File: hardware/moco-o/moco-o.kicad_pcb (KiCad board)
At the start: 4 copper layers, 58 x 52.5 mm, 203 parts, among them J1 USB_C_Receptacle_USB2.0, J10 Conn_01x03, J11 Conn_02x02_Top_Bottom, J12 Conn_02x02_Top_Bottom, J13 Conn_01x02, J2 Conn_02x10_Odd_Even, J3 Conn_01x02, J4 Conn_01x05, J5 SWD 10-Pin, J6 ST-LINK, J8 Conn_01x06, J9 Conn_01x06, Q1 AO3413, Q10 CSD18540Q5B, Q2 AO3413, Q3 CSD18540Q5B, Q4 CSD18540Q5B, Q5 CSD18540Q5B, Q6 CSD18540Q5B, Q7 CSD18540Q5B, Q8 CSD18540Q5B, Q9 CSD18540Q5B, SW1 SW_Push, SW2 SW_Push, SW3 SW_Push, SW4 SW_Push, U1 AMS1117-3.3, U2 DRV8301, U3 8MHz, U4 STM32F405RGTx, U5 TJA1051T-3, U6 LM5109A, U7 AS5047x

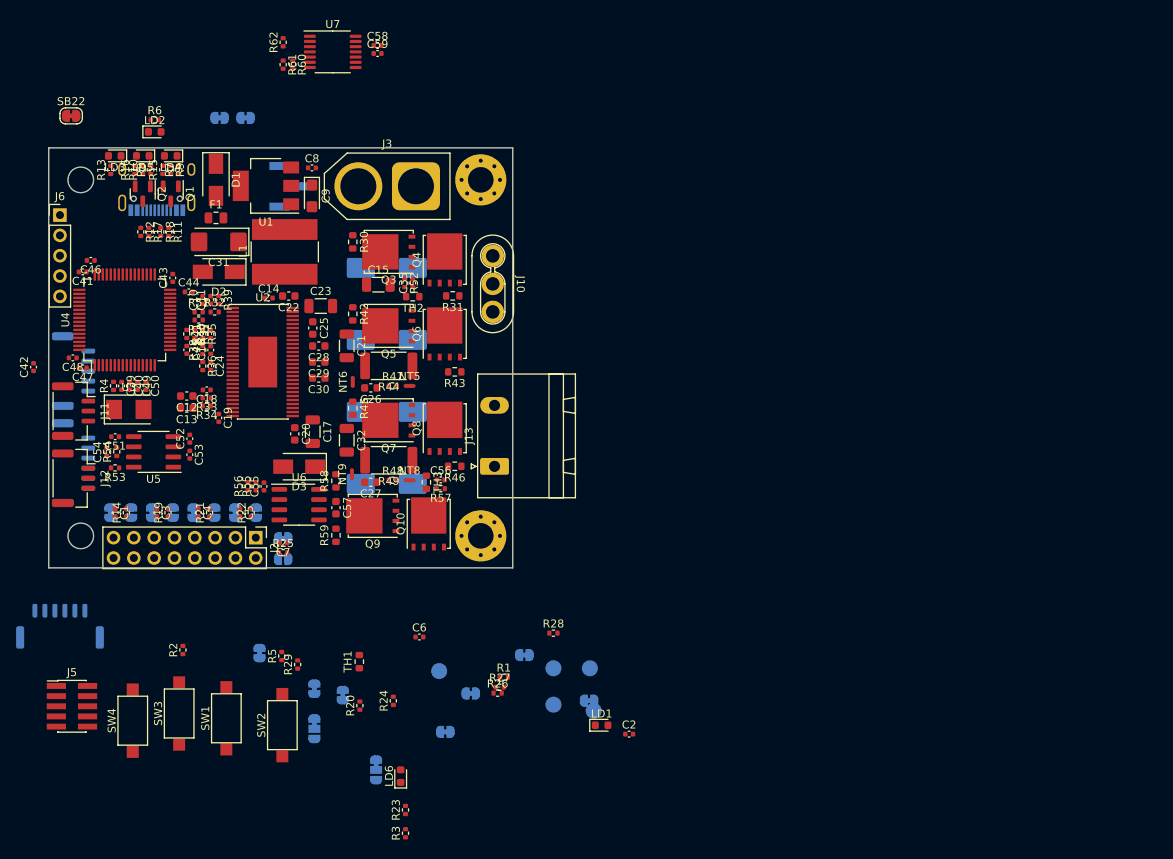
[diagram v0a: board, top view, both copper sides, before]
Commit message: Change to DRV8323H
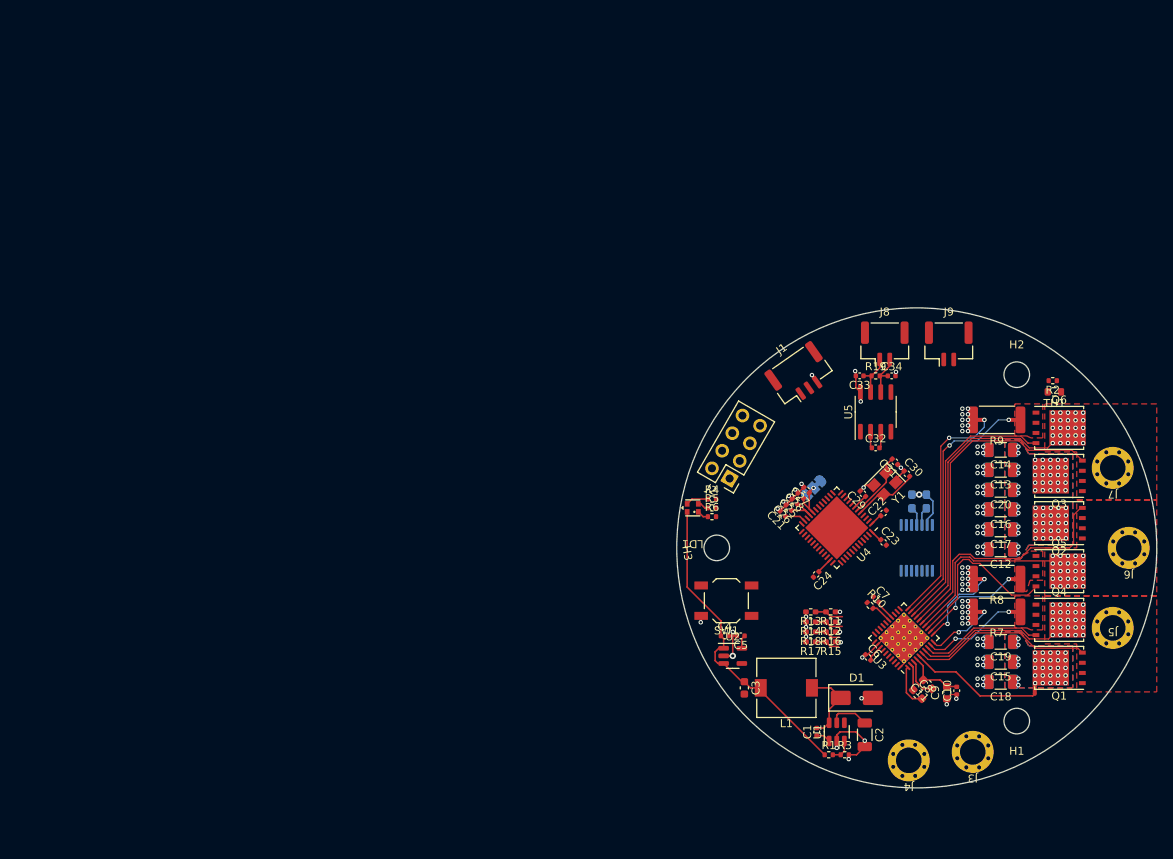
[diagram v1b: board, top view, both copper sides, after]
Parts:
- removed C46: 2.2uF/25V, Capacitor_SMD:C_0402_1005Metric
- removed C47, C48, C49, C51, C53, C59: 100nF, Capacitor_SMD:C_0402_1005Metric
- removed C50: 1uF/25V, Capacitor_SMD:C_0402_1005Metric
- removed C52: 47uF, Capacitor_SMD:C_0402_1005Metric
- removed C54: 100pF, Capacitor_SMD:C_0402_1005Metric
- removed C55, C56: 2.2uF, Capacitor_SMD:C_0402_1005Metric
- removed C57: 100nF/50V, Capacitor_SMD:C_0603_1608Metric
- removed C58: 1uF, Capacitor_SMD:C_0402_1005Metric
- removed D2, D3: SS34, Diode_SMD:D_SMA
- removed F1: 500mA/6V, Fuse:Fuse_0805_2012Metric
- removed H4: MountingHole, MountingHole:MountingHole_3.2mm_M3_ISO14580
- removed J10: Conn_01x03, moco:AMASS MR30PB-F
- removed J11, J12: Conn_02x02_Top_Bottom, Connector_JST:JST_GH_SM03B-GHS-TB_1x03-1MP_P1.25mm_Horizontal
- removed J13: Conn_01x02, Connector_Phoenix_GMSTB:PhoenixContact_GMSTBA_2,5_2-G-7,62_1x02_P7.62mm_Horizontal
- removed JP1: Jumper_3_Open, Connector_PinHeader_2.54mm:PinHeader_1x03_P2.54mm_Vertical_SMD_Pin1Left
- removed LD2, LD3, LD4, LD5, LD6: LED, LED_SMD:LED_0603_1608Metric
- removed NT8, NT9: NetTie_2, NetTie:NetTie-2_SMD_Pad0.5mm
- removed Q10, Q7, Q8, Q9: CSD18540Q5B, Package_TO_SOT_SMD:TDSON-8-1
- removed R20, R23, R35, R37, R41, R52, R53, R57, R60, R61, R62: 10k, Resistor_SMD:R_0402_1005Metric
- removed R21, R22, R25, R26, R27, R28, R38, R51, R55, R56: 3.3k, Resistor_SMD:R_0402_1005Metric
- removed R24, R29, R36: 1k, Resistor_SMD:R_0402_1005Metric
- removed R30, R31, R42, R43, R45, R46, R58, R59: 2.2R, Resistor_SMD:R_0603_1608Metric
- removed R32: 47k, Resistor_SMD:R_0402_1005Metric
- removed R33, R34: 22R, Resistor_SMD:R_0402_1005Metric
- removed R39: 220k 1%, Resistor_SMD:R_0402_1005Metric
- removed R40, R50: 18k, Resistor_SMD:R_0402_1005Metric
- removed R44, R49: 0.5mΩ, Resistor_SMD:R_2512_6332Metric
- removed R47, R48, R54: 120R, Resistor_SMD:R_0402_1005Metric
- removed SB10, SB12, SB14, SB16, SB8: SolderJumper_2_Open, Jumper:SolderJumper-2_P1.3mm_Open_RoundedPad1.0x1.5mm
- removed SB11, SB13, SB15, SB17, SB19, SB2, SB20, SB22, SB3, SB4, SB5, SB6, SB7, SB9: SolderJumper_2_Bridged, Jumper:SolderJumper-2_P1.3mm_Bridged_RoundedPad1.0x1.5mm
- removed SB18, SB21: SolderJumper_3_Bridged12, Jumper:SolderJumper-3_P1.3mm_Bridged12_RoundedPad1.0x1.5mm_NumberLabels
- removed SW2, SW3, SW4: SW_Push, Button_Switch_SMD:SW_SPST_CK_RS282G05A3
- removed TH2, TH3: NCP18XH103F03RB, Resistor_SMD:R_0603_1608Metric
- removed TP1, TP2: TestPoint_Small, TestPoint:TestPoint_Pad_D2.0mm
- removed TP3, TP4, TP5: TestPoint, TestPoint:TestPoint_Pad_D2.0mm
- removed U7: AS5047x, Package_SO:TSSOP-14_4.4x5mm_P0.65mm
- added C38: 10uF/50V, Capacitor_SMD:C_1206_3216Metric_Pad1.33x1.80mm_HandSolder, B.Cu at (160.5, 90.2)
- added J7: C, moco:wire_3.2mm, F.Cu at (174.5, 90.0)
- added NT1: NetTie_2, NetTie:NetTie-2_SMD_Pad0.5mm, F.Cu at (162.0, 108.0)
- added NT2: NetTie_2, NetTie:NetTie-2_SMD_Pad0.5mm, F.Cu at (162.0, 103.9)
- added NT3: NetTie_2, NetTie:NetTie-2_SMD_Pad0.5mm, F.Cu at (162.0, 84.0)
- added NT4: NetTie_2, NetTie:NetTie-2_SMD_Pad0.5mm, F.Cu at (158.0, 108.0)
- added NT7: NetTie_2, NetTie:NetTie-2_SMD_Pad0.5mm, F.Cu at (164.8, 117.8)
- added Y1: 8MHz, Crystal:Crystal_SMD_3225-4Pin_3.2x2.5mm, F.Cu at (146.0, 92.0)
- C1: value 82pF -> 100nF
- C10: value 270pF -> 100nF
- C11: value 82pF -> 1uF/16V; footprint Capacitor_SMD:C_0402_1005Metric -> Capacitor_SMD:C_0603_1608Metric
- C12, C13: value 2.2nF -> 10uF/50V; footprint Capacitor_SMD:C_0603_1608Metric -> Capacitor_SMD:C_1206_3216Metric
- C14: value 15nF -> 10uF/50V; footprint Capacitor_SMD:C_0402_1005Metric -> Capacitor_SMD:C_1206_3216Metric
- C15: value 2.2uF/100V -> 10uF/50V
- C16: value 2.2uF -> 10uF/50V; footprint Capacitor_SMD:C_0402_1005Metric -> Capacitor_SMD:C_1206_3216Metric
- C17: value 4.7uF/50V -> 10uF/50V
- C18, C19: value 1uF -> 10uF/50V; footprint Capacitor_SMD:C_0402_1005Metric -> Capacitor_SMD:C_1206_3216Metric
- C2: value 2.2uF -> 1uF/50V; footprint Capacitor_SMD:C_0402_1005Metric -> Capacitor_SMD:C_1206_3216Metric
- C20: value 100nF/50V -> 10uF/50V; footprint Capacitor_SMD:C_0603_1608Metric -> Capacitor_SMD:C_1206_3216Metric
- C21, C32: value 2.2uF/100V -> 100nF; footprint Capacitor_SMD:C_1206_3216Metric -> Capacitor_SMD:C_0402_1005Metric
- C22, C28, C29: value 100nF/50V -> 100nF; footprint Capacitor_SMD:C_0603_1608Metric -> Capacitor_SMD:C_0402_1005Metric
- C23: value 4.7uF/50V -> 100nF; footprint Capacitor_SMD:C_1206_3216Metric -> Capacitor_SMD:C_0402_1005Metric
- C24: value 22nF -> 100nF
- C25: value 100nF/50V -> 10nF; footprint Capacitor_SMD:C_0603_1608Metric -> Capacitor_SMD:C_0402_1005Metric
- C26, C27: value 2.2nF -> 1uF; footprint Capacitor_SMD:C_0603_1608Metric -> Capacitor_SMD:C_0402_1005Metric
- C3: value 82pF -> 10uF; footprint Capacitor_SMD:C_0402_1005Metric -> Capacitor_SMD:C_0603_1608Metric
- C30: value 100nF/50V -> 12pF; footprint Capacitor_SMD:C_0603_1608Metric -> Capacitor_SMD:C_0402_1005Metric
- C31: value 68uF -> 12pF; footprint Capacitor_Tantalum_SMD:CP_EIA-6032-28_Kemet-C -> Capacitor_SMD:C_0402_1005Metric
- C33, C34: value 47uF/63V -> 30pF; footprint Capacitor_SMD:CP_Elec_8x10 -> Capacitor_SMD:C_0402_1005Metric; moved to F.Cu
- C35: value 2.2uF -> 100nF; footprint Capacitor_SMD:C_0402_1005Metric -> Capacitor_SMD:C_0603_1608Metric_Pad1.08x0.95mm_HandSolder; moved to B.Cu
- C36: value 47uF/63V -> 1uF; footprint Capacitor_SMD:CP_Elec_8x10 -> Capacitor_SMD:C_0603_1608Metric_Pad1.08x0.95mm_HandSolder
- C37: value 47uF/63V -> 10uF/50V; footprint Capacitor_SMD:CP_Elec_8x10 -> Capacitor_SMD:C_1206_3216Metric_Pad1.33x1.80mm_HandSolder
- C39, C40: value 20pF -> 10uF/50V; footprint Capacitor_SMD:C_0402_1005Metric -> Capacitor_SMD:C_1206_3216Metric_Pad1.33x1.80mm_HandSolder; moved to B.Cu
- C4, C5: value 82pF -> 1uF
- C41, C42, C43, C45: value 100nF -> 10uF/50V; footprint Capacitor_SMD:C_0402_1005Metric -> Capacitor_SMD:C_1206_3216Metric_Pad1.33x1.80mm_HandSolder; moved to B.Cu
- C44: value 2.2uF/25V -> 10uF/50V; footprint Capacitor_SMD:C_0402_1005Metric -> Capacitor_SMD:C_1206_3216Metric_Pad1.33x1.80mm_HandSolder; moved to B.Cu
- C6: value 270pF -> 1uF/6.3V
- C7: value 82pF -> 100nF/6.3V
- C8: value 10uF -> 47nF; footprint Capacitor_SMD:C_0402_1005Metric -> Capacitor_SMD:C_0603_1608Metric
- C9: footprint Capacitor_Tantalum_SMD:CP_EIA-3216-18_Kemet-A -> Capacitor_SMD:C_0603_1608Metric
- H1, H2: value MountingHole_Pad -> MountingHole; footprint MountingHole:MountingHole_3.2mm_M3_Pad_Via -> MountingHole:MountingHole_3.2mm_M3_ISO14580
- J1: value USB_C_Receptacle_USB2.0 -> Serial; footprint Connector_USB:USB_C_Receptacle_HRO_TYPE-C-31-M-12 -> Connector_JST:JST_GH_BM03B-GHS-TBT_1x03-1MP_P1.25mm_Vertical; moved to F.Cu
- J2: value Conn_02x10_Odd_Even -> Debug; footprint Connector_PinHeader_2.54mm:PinHeader_2x08_P2.54mm_Vertical -> Connector_PinHeader_2.54mm:PinHeader_2x04_P2.54mm_Vertical
- J3: value Conn_01x02 -> A; footprint Connector_AMASS:AMASS_XT60-M_1x02_P7.20mm_Vertical -> moco:wire_3.2mm
- J4: value Conn_01x05 -> A; footprint Connector_JST:JST_GH_SM05B-GHS-TB_1x05-1MP_P1.25mm_Horizontal -> moco:wire_3.2mm; moved to F.Cu
- J5: value SWD 10-Pin -> A; footprint Connector_PinHeader_1.27mm:PinHeader_2x05_P1.27mm_Vertical_SMD -> moco:wire_3.2mm
- J6: value ST-LINK -> B; footprint Connector_PinHeader_2.54mm:PinHeader_1x05_P2.54mm_Vertical -> moco:wire_3.2mm
- J8: value Conn_01x06 -> CAN1; footprint Connector_JST:JST_GH_SM06B-GHS-TB_1x06-1MP_P1.25mm_Horizontal -> Connector_JST:JST_GH_BM02B-GHS-TBT_1x02-1MP_P1.25mm_Vertical; moved to F.Cu
- J9: value Conn_01x06 -> CAN2; footprint Connector_JST:JST_GH_BM06B-GHS-TBT_1x06-1MP_P1.25mm_Vertical -> Connector_JST:JST_GH_BM02B-GHS-TBT_1x02-1MP_P1.25mm_Vertical; moved to F.Cu
- L1: value 22uH/1.5A -> 22uH; footprint Inductor_SMD:L_Bourns-SRN8040_8x8.15mm -> Inductor_SMD:L_7.3x7.3_H3.5
- LD1: value LED -> LED_BAGR; footprint LED_SMD:LED_0603_1608Metric -> moco:RGB LED 1.6x1.6mm
- Q1, Q2: value AO3413 -> CSD18540Q5B; footprint Package_TO_SOT_SMD:SOT-23 -> Package_TO_SOT_SMD:TDSON-8-1
- R1: value 10k -> 54.9k
- R11: value 5.1k -> DNI; footprint Resistor_SMD:R_0402_1005Metric -> Resistor_SMD:R_0402_1005Metric_Pad0.72x0.64mm_HandSolder
- R12: value 5.1k -> 0R; footprint Resistor_SMD:R_0402_1005Metric -> Resistor_SMD:R_0402_1005Metric_Pad0.72x0.64mm_HandSolder
- R13: value 1k -> 0R; footprint Resistor_SMD:R_0402_1005Metric -> Resistor_SMD:R_0402_1005Metric_Pad0.72x0.64mm_HandSolder
- R14: value 3.3k -> DNI; footprint Resistor_SMD:R_0402_1005Metric -> Resistor_SMD:R_0402_1005Metric_Pad0.72x0.64mm_HandSolder
- R15: value 330R -> DNI; footprint Resistor_SMD:R_0402_1005Metric -> Resistor_SMD:R_0402_1005Metric_Pad0.72x0.64mm_HandSolder
- R16: value 330R -> 0R; footprint Resistor_SMD:R_0402_1005Metric -> Resistor_SMD:R_0402_1005Metric_Pad0.72x0.64mm_HandSolder
- R17: value 22R -> 47k; footprint Resistor_SMD:R_0402_1005Metric -> Resistor_SMD:R_0402_1005Metric_Pad0.72x0.64mm_HandSolder
- R18: value 22R -> DNI; footprint Resistor_SMD:R_0402_1005Metric -> Resistor_SMD:R_0402_1005Metric_Pad0.72x0.64mm_HandSolder
- R19: value 3.3k -> 120R
- R4: value 10k -> 1k
- R5: value 1k -> 5k
- R7, R8: value 150R -> 0.5mΩ; footprint Resistor_SMD:R_0402_1005Metric -> Resistor_SMD:R_2512_6332Metric
- R9: value 10k -> 0.5mΩ; footprint Resistor_SMD:R_0402_1005Metric -> Resistor_SMD:R_2512_6332Metric
- SB1: value SolderJumper_2_Bridged -> SolderJumper_3_Bridged12; footprint Jumper:SolderJumper-2_P1.3mm_Bridged_RoundedPad1.0x1.5mm -> Jumper:SolderJumper-3_P1.3mm_Bridged12_RoundedPad1.0x1.5mm
- SW1: value SW_Push -> RESET; footprint Button_Switch_SMD:SW_SPST_CK_RS282G05A3 -> Button_Switch_SMD:SW_SPST_TL3342
- U1: value AMS1117-3.3 -> LMR16006X; footprint Package_TO_SOT_SMD:SOT-223-3_TabPin2 -> Package_TO_SOT_SMD:SOT-23-6
- U2: value DRV8301 -> RT9013-33GB; footprint Package_SO:HTSSOP-56-1EP_6.1x14mm_P0.5mm_EP3.61x6.35mm -> Package_TO_SOT_SMD:SOT-23-5
- U3: value 8MHz -> DRV8323H; footprint Crystal:Crystal_SMD_5032-2Pin_5.0x3.2mm -> Package_DFN_QFN:QFN-40-1EP_6x6mm_P0.5mm_EP4.6x4.6mm_ThermalVias
- U4: value STM32F405RGTx -> STM32G431CBUx; footprint Package_QFP:LQFP-64_10x10mm_P0.5mm -> Package_DFN_QFN:QFN-48-1EP_7x7mm_P0.5mm_EP5.6x5.6mm
- U5: value TJA1051T-3 -> TJA1050
- U6: value LM5109A -> AS5047x; footprint Package_SO:SOIC-8_3.9x4.9mm_P1.27mm -> Package_SO:TSSOP-14_4.4x5mm_P0.65mm; moved to B.Cu
- moved J6 139.9 mm to (176.5, 100.0), turned to 180 degrees
- moved J5 130.5 mm to (174.5, 110.0), turned to 180 degrees
- moved Q1 125.9 mm to (167.8, 115.0), turned to 180 degrees
- moved C42 123.0 mm to (160.5, 100.2), turned to 180 degrees
- moved Q2 121.7 mm to (167.8, 96.9), turned to 180 degrees
- moved C41 119.2 mm to (160.5, 97.7)
- moved R8 117.5 mm to (160.0, 103.9), turned to 180 degrees
- moved J9 116.6 mm to (154.0, 74.5)
- moved R7 116.2 mm to (160.0, 108.0), turned to 180 degrees
- moved J4 115.2 mm to (149.0, 126.6), turned to 180 degrees
- moved R2 113.8 mm to (167.0, 79.1), turned to 180 degrees
- moved C43 113.1 mm to (160.5, 111.8), turned to 180 degrees
- moved C44 111.5 mm to (160.5, 114.2), turned to 180 degrees
- moved C39 110.7 mm to (160.5, 92.8), turned to 180 degrees
- moved C40 110.0 mm to (160.5, 95.2), turned to 180 degrees
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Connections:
- C1 pad 1: Net-(C1-Pad1) -> Net-(U1-CB)
- C1 pad 2: GND -> Net-(D1-K)
- C10 pad 1: Net-(C10-Pad1) -> GND
- C10 pad 2: GND -> Vdrive
- C11 pad 1: Net-(C11-Pad1) -> Net-(U3-VCP)
- C11 pad 2: GND -> Vdrive
- C12 pad 1: /MCU/M0_CUR_SENSE_1 -> Vdrive
- C13 pad 1: /MCU/M0_CUR_SENSE_2 -> Vdrive
- C14 pad 1: GND -> Vdrive
- C14 pad 2: Net-(C14-Pad2) -> GND
- C16 pad 1: GATE_VDD -> Vdrive
- C18 pad 1: Net-(C18-Pad1) -> Vdrive
- C19 pad 1: Net-(C19-Pad1) -> Vdrive
- C2 pad 1: /POWER_TEMP -> Vdrive
- C21 pad 1: Vdrive -> +3.3V
- C22 pad 1: Vdrive -> +3.3V
- C23 pad 1: Vdrive -> +3.3V
- C24 pad 1: Net-(C24-Pad1) -> +3.3V
- C24 pad 2: Net-(C24-Pad2) -> GND
- C25 pad 1: Net-(C25-Pad1) -> +3.3V
- C25 pad 2: Net-(C25-Pad2) -> GND
- C26 pad 1: Net-(C26-Pad1) -> +3.3V
- C26 pad 2: /Motor Driver/SP1 -> GND
- C27 pad 1: Net-(C27-Pad1) -> Net-(SB1-C)
- C27 pad 2: /Motor Driver/SP2 -> GND
- C28 pad 1: /Motor Driver/MOTOR_A -> Net-(SB1-C)
- C28 pad 2: Net-(C28-Pad2) -> GND
- C29 pad 1: /Motor Driver/MOTOR_B -> /~{RESET}
- C29 pad 2: Net-(C29-Pad2) -> GND
- C3 pad 1: Net-(C3-Pad1) -> +5V
- C30 pad 1: /Motor Driver/MOTOR_C -> GND
- C30 pad 2: Net-(C30-Pad2) -> /MCU/OSC_IN
- C31 pad 1: +5V -> GND
- C31 pad 2: GND -> /MCU/OSC_OUT
- C32 pad 1: Vdrive -> GND
- C32 pad 2: GND -> +5V
- C33 pad 1: Vdrive -> /CAN Bus/CAN_H
- C34 pad 1: Vdrive -> /CAN Bus/CAN_L
- C35 pad 1: /MCU/M0_TEMP -> +3.3V
- C36 pad 1: Vdrive -> +3.3V
- C39 pad 1: GND -> Vdrive
- C39 pad 2: Net-(C39-Pad2) -> GND
- C4 pad 1: Net-(C4-Pad1) -> +5V
- C40 pad 1: GND -> Vdrive
- C40 pad 2: Net-(C40-Pad2) -> GND
- C41 pad 1: VCC -> Vdrive
- C42 pad 1: /MCU_~{RESET} -> Vdrive
- C43 pad 1: VCC -> Vdrive
- C44 pad 1: Net-(C44-Pad1) -> Vdrive
- C45 pad 1: VCC -> Vdrive
- C5 pad 1: Net-(C5-Pad1) -> +3.3V
- C6 pad 1: /MCU/VBUS_S -> GND
- C6 pad 2: GND -> VDD
- C7 pad 1: Net-(C7-Pad1) -> GND
- C7 pad 2: GND -> /MCU/VREF
- C8 pad 1: +5V -> Net-(U3-CPH)
- C8 pad 2: GND -> Net-(U3-CPL)
- C9 pad 1: VCC -> GND
- C9 pad 2: GND -> Vdrive
- D1 pad 1: Net-(D1-Pad1) -> Net-(D1-K)
- D1 pad 2: Net-(D1-Pad2) -> GND
- J2 pad 1: +5V -> +3.3V
- J2 pad 2: VCC -> +5V
- J2 pad 3: /PA0_CONN -> /UART1_TX
- J2 pad 4: /PA1_CONN -> /SWCLK
- J2 pad 5: /PA2 -> /UART1_RX
- J2 pad 6: /PA3 -> /SWDIO
- J2 pad 7: /PA7 -> GND
- J2 pad 8: /PA15_CONN -> GND
- J3 pad 1: GND -> Vdrive
- J4 pad 1: Net-(J4-Pad1) -> GND
- J5 pad 1: VCC -> /Motor Driver/OUTA
- J6 pad 1: VCC -> /Motor Driver/OUTB
- J8 pad 1: Net-(J8-Pad1) -> /CAN Bus/CAN_H
- J8 pad 2: /SPI_CLK -> /CAN Bus/CAN_L
- J9 pad 1: /AS5047x_A -> /CAN Bus/CAN_H
- J9 pad 2: /AS5047x_B -> /CAN Bus/CAN_L
- L1 pad 1: Net-(C25-Pad2) -> Net-(D1-K)
- LD1 pad 1: GND -> Net-(LD1-BK)
- LD1 pad 2: Net-(LD1-Pad2) -> +5V
- NT5 pad 1: /Motor Driver/SN1 -> /Motor Driver/SNB
- NT5 pad 2: /Motor Driver/SL_B -> GND
- NT6 pad 1: /Motor Driver/SP1 -> /Motor Driver/SNC
- Q1 pad 1: Net-(Q1-Pad1) -> /Motor Driver/OUTA
- Q1 pad 2: Net-(Q1-Pad2) -> /Motor Driver/OUTA
- Q1 pad 3: Net-(Q1-Pad3) -> /Motor Driver/OUTA
- Q2 pad 1: Net-(Q2-Pad1) -> /Motor Driver/OUTB
- Q2 pad 2: Net-(Q2-Pad2) -> /Motor Driver/OUTB
- Q2 pad 3: Net-(Q2-Pad3) -> /Motor Driver/OUTB
- Q3 pad 1: /Motor Driver/MOTOR_A -> /Motor Driver/OUTC
- Q3 pad 2: /Motor Driver/MOTOR_A -> /Motor Driver/OUTC
- Q3 pad 3: /Motor Driver/MOTOR_A -> /Motor Driver/OUTC
- Q3 pad 4: Net-(Q3-Pad4) -> /Motor Driver/GHC
- Q4 pad 1: GND -> Net-(NT1-Pad2)
- Q4 pad 2: GND -> Net-(NT1-Pad2)
- Q4 pad 3: GND -> Net-(NT1-Pad2)
- Q4 pad 4: Net-(Q4-Pad4) -> /Motor Driver/GLA
- Q4 pad 5: /Motor Driver/MOTOR_A -> /Motor Driver/OUTA
- Q5 pad 1: /Motor Driver/MOTOR_B -> Net-(NT2-Pad2)
- Q5 pad 2: /Motor Driver/MOTOR_B -> Net-(NT2-Pad2)
- Q5 pad 3: /Motor Driver/MOTOR_B -> Net-(NT2-Pad2)
- Q5 pad 4: Net-(Q5-Pad4) -> /Motor Driver/GLB
- Q5 pad 5: Vdrive -> /Motor Driver/OUTB
- Q6 pad 1: /Motor Driver/SL_B -> Net-(NT3-Pad2)
- Q6 pad 2: /Motor Driver/SL_B -> Net-(NT3-Pad2)
- Q6 pad 3: /Motor Driver/SL_B -> Net-(NT3-Pad2)
- Q6 pad 4: Net-(Q6-Pad4) -> /Motor Driver/GLC
- Q6 pad 5: /Motor Driver/MOTOR_B -> /Motor Driver/OUTC
- R1 pad 1: Net-(R1-Pad1) -> +5V
- R1 pad 2: GND -> Net-(U1-FB)
- R10 pad 1: Net-(Q2-Pad1) -> +3.3V
- R10 pad 2: Net-(Q2-Pad2) -> /MCU/~{FAULT}
- R11 pad 1: Net-(J1-PadA5) -> VDD
- R11 pad 2: GND -> /Motor Driver/MODE
- R12 pad 1: Net-(J1-PadB5) -> VDD
- R12 pad 2: GND -> /Motor Driver/IDRIVE
- R13 pad 1: Net-(R13-Pad1) -> /Motor Driver/MODE
- R13 pad 2: Net-(LD3-Pad2) -> GND
- R14 pad 1: /PA0_CONN -> /Motor Driver/IDRIVE
- R14 pad 2: /PA0 -> GND
- R15 pad 1: Net-(Q1-Pad3) -> VDD
- R15 pad 2: Net-(LD4-Pad2) -> /Motor Driver/GAIN
- R16 pad 1: Net-(Q2-Pad3) -> VDD
- R16 pad 2: Net-(LD5-Pad2) -> /Motor Driver/VDS
- R17 pad 1: Net-(J1-PadA7) -> /Motor Driver/GAIN
- R17 pad 2: /USB_D- -> GND
- R18 pad 1: Net-(J1-PadA6) -> /Motor Driver/VDS
- R18 pad 2: /USB_D+ -> GND
- R19 pad 1: /PA1_CONN -> /CAN Bus/CAN_H
- R19 pad 2: /PA1 -> /CAN Bus/CAN_L
- R2 pad 1: Net-(R2-Pad1) -> GND
- R2 pad 2: GND -> /TEMP_SENSOR
- R3 pad 1: /MCU_BOOT0 -> Net-(U1-FB)
- R4 pad 1: VCC -> Net-(LD1-RK)
- R4 pad 2: /MCU_~{RESET} -> /USER_LED1
- R5 pad 1: Net-(R5-Pad1) -> Net-(LD1-GK)
- R5 pad 2: Net-(LD1-Pad2) -> GND
- R6 pad 1: Net-(R6-Pad1) -> Net-(LD1-BK)
- R6 pad 2: Net-(LD2-Pad2) -> /USER_LED2
- R7 pad 1: Net-(Q1-Pad1) -> Net-(NT1-Pad2)
- R7 pad 2: /~{FAULT} -> GND
- R8 pad 1: Net-(Q2-Pad1) -> Net-(NT2-Pad2)
- R8 pad 2: /~{OCTW} -> GND
- R9 pad 1: Net-(Q1-Pad1) -> Net-(NT3-Pad2)
- R9 pad 2: Net-(Q1-Pad2) -> GND
- SB1 pad 1: Net-(R1-Pad1) -> +3.3V
- SB1 pad 2: /USER_Button2 -> Net-(SB1-C)
- SW1 pad 1: Net-(R1-Pad1) -> GND
- SW1 pad 2: VCC -> /~{RESET}
- TH1 pad 1: VCC -> +3.3V
- TH1 pad 2: /POWER_TEMP -> /TEMP_SENSOR
- U1 pad 1: GND -> Net-(U1-CB)
- U1 pad 2: VCC -> GND
- U1 pad 3: +5V -> Net-(U1-FB)
- U2 pad 1: Net-(R39-Pad2) -> +5V
- U2 pad 2: Net-(C11-Pad1) -> GND
- U2 pad 3: /Motor Driver/V_SENSE -> +5V
- U2 pad 4: /Motor Driver/PWRGD -> unconnected-(U2-NC-Pad4)
- U2 pad 5: /~{OCTW} -> +3.3V
- U3 pad 1: Net-(C39-Pad2) -> Net-(U3-CPL)
- U3 pad 2: Net-(C40-Pad2) -> Net-(U3-CPH)
- U4 pad 1: VCC -> +3.3V
- U4 pad 10: /USER_Button1 -> /UART2_TX
- U4 pad 11: /USER_Button2 -> /UART2_RX
- U4 pad 12: GND -> unconnected-(U4-PA4-Pad12)
- U4 pad 13: VCC -> /MCU/CS_A
- U4 pad 14: /PA0 -> /MCU/CS_B
- U4 pad 15: /PA1 -> /MCU/CS_C
- U4 pad 16: /PA2 -> /MCU/~{FAULT}
- U4 pad 17: /PA3 -> /USER_LED1
- U4 pad 18: GND -> /USER_LED2
- U4 pad 19: VCC -> /SPI_~{CS}_AS5047
- U4 pad 2: /SPI_~{CS}_DRV8301 -> unconnected-(U4-PC13-Pad2)
- U4 pad 20: /POWER_TEMP -> Net-(SB1-C)
- U4 pad 21: /Braking Circuit/TEMP_SENSE -> +3.3V
- U4 pad 22: /MCU/VBUS_S -> unconnected-(U4-PB10-Pad22)
- U4 pad 23: /PA7 -> +3.3V
- U4 pad 24: /PC4 -> unconnected-(U4-PB11-Pad24)
- U4 pad 25: /MCU/M0_TEMP -> /TEMP_SENSOR
- U4 pad 26: /PB0 -> /MCU/PWM_LA
- U4 pad 27: /PB1 -> /MCU/PWM_LB
- U4 pad 28: /PB2 -> /MCU/PWM_LC
- U4 pad 29: /Braking Circuit/LI -> /MCU/GATE_ENABLE
- U4 pad 3: /SPI_~{CS}_AS5047x -> unconnected-(U4-PC14-Pad3)
- U4 pad 30: /Braking Circuit/HI -> /MCU/PWM_HA
- U4 pad 31: Net-(C44-Pad1) -> /MCU/PWM_HB
- U4 pad 32: VCC -> /MCU/PWM_HC
- U4 pad 33: /EN_GATE -> /CAN_RX
- U4 pad 34: /MCU/M0_AL -> /CAN_TX
- U4 pad 35: /MCU/M0_BL -> +3.3V
- U4 pad 36: /MCU/M0_CL -> /SWDIO
- U4 pad 37: /USER_LED1 -> /SWCLK
- U4 pad 38: /USER_LED2 -> unconnected-(U4-PA15-Pad38)
- U4 pad 39: /PC8 -> /MCU/AMP_CAL
- U4 pad 4: /AS5047x_I -> unconnected-(U4-PC15-Pad4)
- U4 pad 40: /ENC_Z -> unconnected-(U4-PC11-Pad40)
- U4 pad 41: /MCU/M0_AH -> /SPI_SCLK
- U4 pad 42: /MCU/M0_BH -> /SPI_MISO
- U4 pad 43: /MCU/M0_CH -> /SPI_MOSI
- U4 pad 44: /USB_D+ -> /UART1_TX
- U4 pad 45: /USB_D- -> /UART1_RX
- U4 pad 46: /SWDIO -> /BOOT0
- U4 pad 47: Net-(C46-Pad1) -> unconnected-(U4-PB9-Pad47)
- U4 pad 48: VCC -> +3.3V
- U4 pad 49: /SWCLK -> GND
- U4 pad 5: Net-(C39-Pad2) -> /MCU/OSC_IN
- U4 pad 6: Net-(C40-Pad2) -> /MCU/OSC_OUT
- U4 pad 7: /MCU_~{RESET} -> /~{RESET}
- U4 pad 8: /MCU/M0_CUR_SENSE_1 -> unconnected-(U4-PA0-Pad8)
- U4 pad 9: /MCU/M0_CUR_SENSE_2 -> unconnected-(U4-PA1-Pad9)
- U5 pad 1: /CNA_TX -> /CAN_TX
- U5 pad 4: /CNA_RX -> /CAN_RX
- U5 pad 5: VCC -> unconnected-(U5-VREF-Pad5)
- U5 pad 6: /CAN BUS/CAN_L -> /CAN Bus/CAN_L
- U5 pad 7: /CAN BUS/CAN_H -> /CAN Bus/CAN_H
- U5 pad 8: Net-(R53-Pad1) -> GND
- U6 pad 1: GATE_VDD -> /SPI_~{CS}_AS5047
- U6 pad 2: /Braking Circuit/HI -> /SPI_SCLK
- U6 pad 3: /Braking Circuit/LI -> /SPI_MISO
- U6 pad 4: GND -> /SPI_MOSI
- U6 pad 5: Net-(R59-Pad2) -> GND
- U6 pad 6: Net-(C57-Pad2) -> /AS5047_B
- U6 pad 7: Net-(R58-Pad2) -> /AS5047_A
- U6 pad 8: Net-(C57-Pad1) -> /Angle Sensor/W/PWM
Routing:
- net GND: track 0.00 -> 61.5 mm, vias 0 -> 91
- net +5V: track 0.00 -> 42.2 mm
- net /Motor Driver/GHC: track 0.00 -> 39.9 mm
- net /Motor Driver/OUTC: track 0.00 -> 38.7 mm, vias 0 -> 25
- net /Motor Driver/GLC: track 0.00 -> 33.8 mm
- net /Motor Driver/SPC: track 0.00 -> 31.6 mm, vias 0 -> 2
- net /Motor Driver/GHB: track 0.00 -> 30.8 mm
- net /Motor Driver/SNC: track 0.00 -> 29.4 mm, vias 0 -> 2
- net /Motor Driver/OUTB: track 0.00 -> 24.9 mm, vias 0 -> 25
- net /Motor Driver/GHA: track 0.00 -> 22.8 mm
- net /Motor Driver/GLB: track 0.00 -> 21.9 mm
- net /Motor Driver/OUTA: track 0.00 -> 20.9 mm, vias 0 -> 25
- net +3.3V: track 0.00 -> 18.8 mm
- net Net-(U3-VDRAIN): track 0.00 -> 16.6 mm
- net /Motor Driver/GLA: track 0.00 -> 15.5 mm
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- added copper zone on F.Cu, net /Motor Driver/OUTA
- added copper zone on F.Cu, net /Motor Driver/OUTB
- added copper zone on F.Cu, net /Motor Driver/OUTC
- added copper zone on F.Cu, net Net-(NT1-Pad2)
- added copper zone on F.Cu, net Net-(NT2-Pad2)
- added copper zone on F.Cu, net Net-(NT3-Pad2)
- added copper zone on B.Cu, net Vdrive
- added copper zone on F.Cu, net Vdrive
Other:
- board size 58 x 52.5 mm -> 60 x 60 mm
